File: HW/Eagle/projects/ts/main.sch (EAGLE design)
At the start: 29 parts, among them IC1 4050D, U1 ATMEGA328P-PU, U2 LM2576T, U3 HT7533

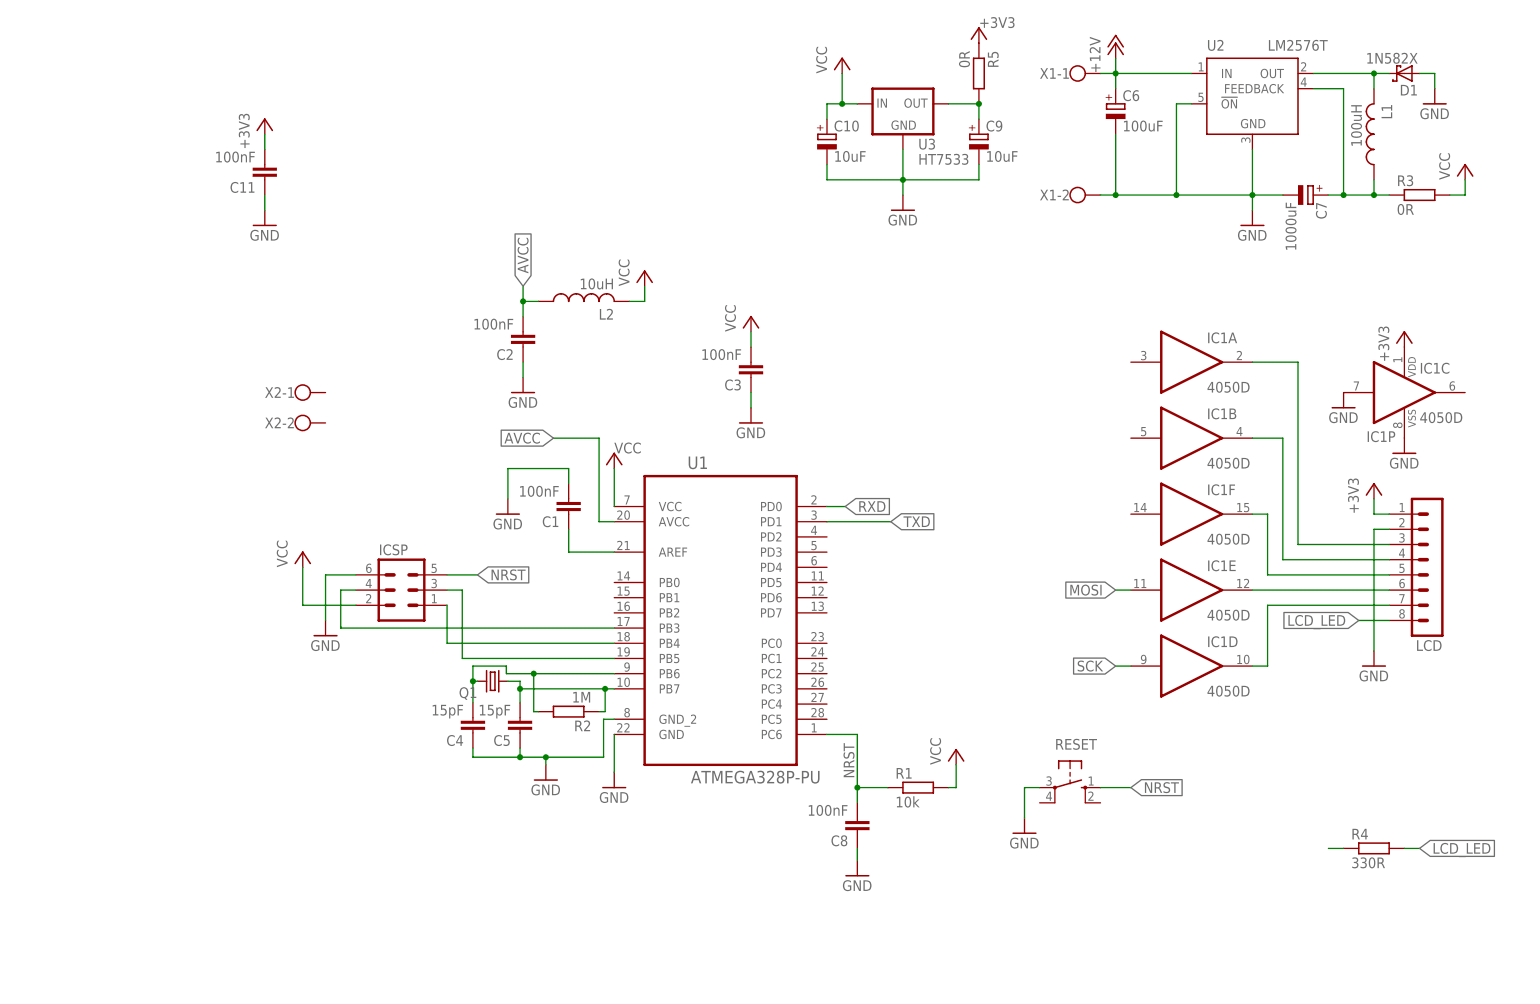
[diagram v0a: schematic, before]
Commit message: Commit before changing to digital temperature sensor
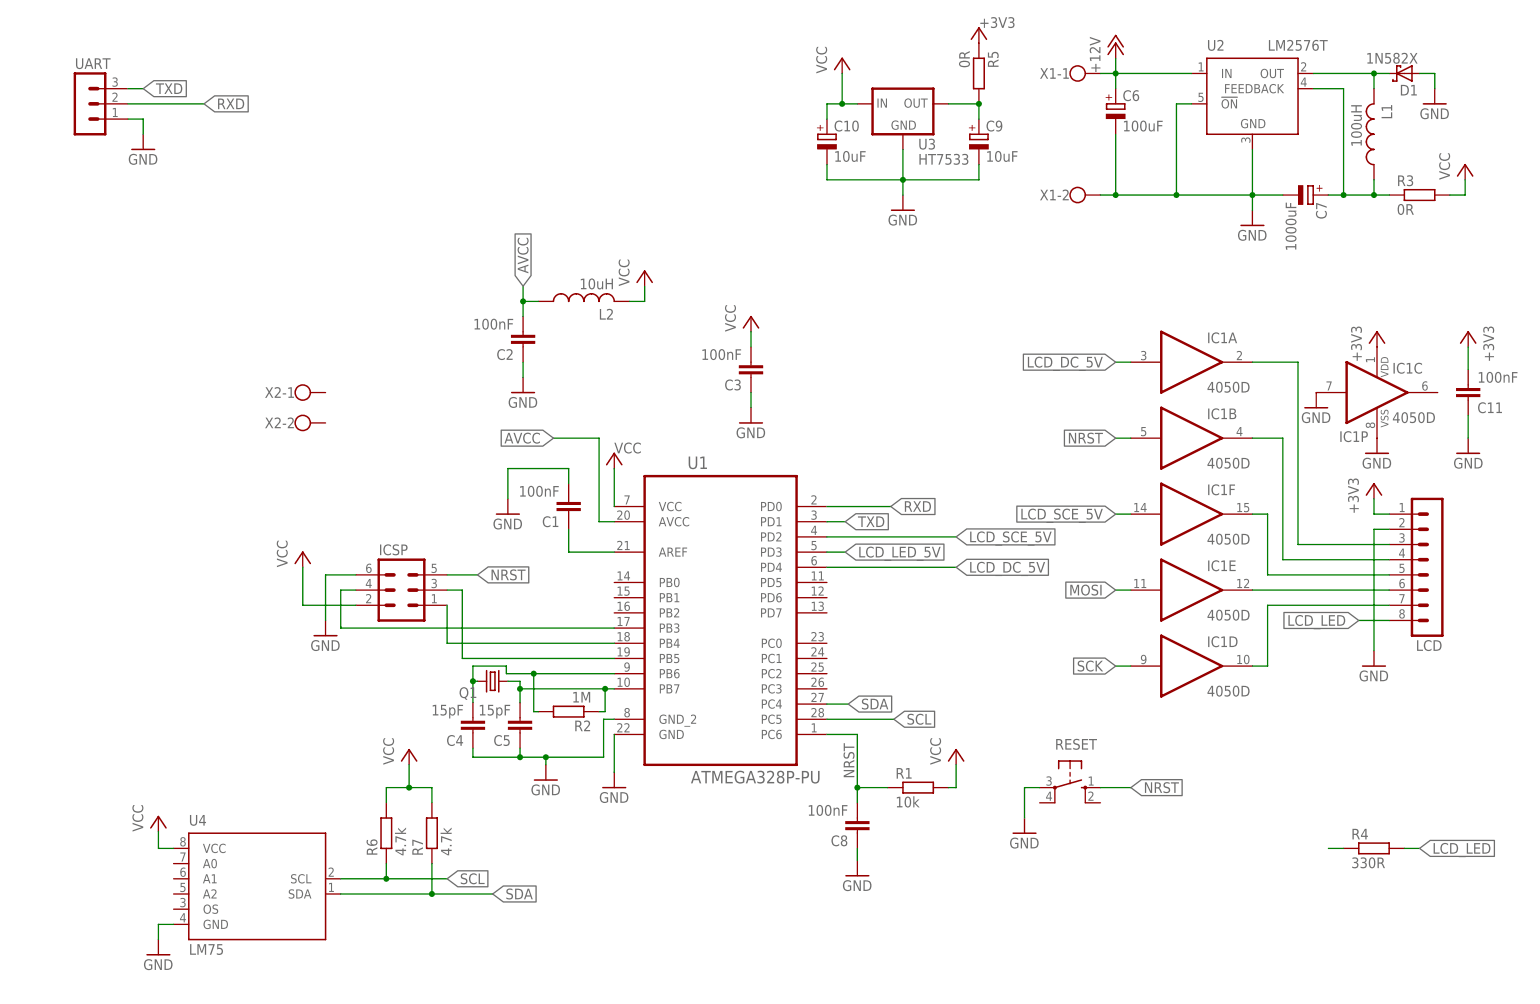
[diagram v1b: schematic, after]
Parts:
- added R6, R7: 4.7k, rcl:R-EU_R0805
- added U4: LM75, misc:LM75
- added UART: (no value), con-lstb:MA03-1
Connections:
- new net LCD_DC_5V: IC1A.I, U1.PD4
- new net LCD_LED_5V: U1.PD3
- new net LCD_SCE_5V: IC1F.I, U1.PD2
- new net SCL: R6.1, U1.PC5, U4.SCL
- new net SDA: R7.1, U1.PC4, U4.SDA
- net GND: now also U4.GND, UART.1
- net NRST: now also IC1B.I
- net RXD: now also UART.2
- net TXD: now also UART.3
- net VCC: now also R6.2, R7.2, U4.VCC
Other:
- moved on the sheet: C11, IC1C, IC1P
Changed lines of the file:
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@@
 <part name="GND14" library="supply1" deviceset="GND" device=""/>
 <part name="GND15" library="supply1" deviceset="GND" device=""/>
+<part name="UART" library="con-lstb" deviceset="MA03-1" device=""/>
+<part name="GND16" library="supply1" deviceset="GND" device=""/>
+<part name="U4" library="misc" deviceset="LM75" device=""/>
+<part name="R6" library="rcl" deviceset="R-EU_" device="R0805" value="4.7k"/>
+<part name="R7" library="rcl" deviceset="R-EU_" device="R0805" value="4.7k"/>
+<part name="P+9" library="supply1" deviceset="VCC" device=""/>
+<part name="P+10" library="supply1" deviceset="VCC" device=""/>
+<part name="GND17" library="supply1" deviceset="GND" device=""/>
 </parts>
 <sheets>
@@
 <instance part="IC1" gate="A" x="200.66" y="111.76"/>
 <instance part="IC1" gate="B" x="200.66" y="99.06"/>
-<instance part="IC1" gate="C" x="236.22" y="106.68"/>
+<instance part="IC1" gate="C" x="231.648" y="106.68"/>
 <instance part="IC1" gate="D" x="200.66" y="60.96"/>
 <instance part="IC1" gate="E" x="200.66" y="73.66"/>
 <instance part="IC1" gate="F" x="200.66" y="86.36"/>
-<instance part="IC1" gate="P" x="236.22" y="106.68" smashed="yes">
-<attribute name="NAME" x="229.87" y="98.425" size="1.778" layer="95"/>
+<instance part="IC1" gate="P" x="231.648" y="106.68" smashed="yes">
+<attribute name="NAME" x="225.298" y="98.425" size="1.778" layer="95"/>
 </instance>
-<instance part="GND9" gate="1" x="236.22" y="96.52"/>
-<instance part="+3V2" gate="G$1" x="236.22" y="116.84"/>
+<instance part="GND9" gate="1" x="231.648" y="96.52"/>
+<instance part="+3V2" gate="G$1" x="231.648" y="116.84"/>
 <instance part="LCD" gate="1" x="241.3" y="78.74" rot="R180"/>
 <instance part="+3V3" gate="G$1" x="231.14" y="91.44"/>
@@
 <instance part="GND11" gate="1" x="88.9" y="106.68"/>
 <instance part="GND12" gate="1" x="86.36" y="86.36"/>
-<instance part="C11" gate="G$1" x="45.72" y="142.24" rot="R180"/>
-<instance part="+3V4" gate="G$1" x="45.72" y="152.4"/>
-<instance part="GND13" gate="1" x="45.72" y="134.62"/>
+<instance part="C11" gate="G$1" x="246.888" y="105.41" rot="MR180"/>
+<instance part="+3V4" gate="G$1" x="246.888" y="116.84" rot="MR0"/>
+<instance part="GND13" gate="1" x="246.888" y="96.52" rot="MR0"/>
 <instance part="R4" gate="G$1" x="231.14" y="30.48"/>
 <instance part="RESET" gate="1" x="180.34" y="40.64" rot="R270"/>
 <instance part="GND14" gate="1" x="172.72" y="33.02"/>
-<instance part="GND15" gate="1" x="226.06" y="104.14"/>
+<instance part="GND15" gate="1" x="221.488" y="104.14"/>
+<instance part="UART" gate="G$1" x="15.24" y="154.94"/>
+<instance part="GND16" gate="1" x="25.4" y="147.32"/>
+<instance part="U4" gate="G$1" x="43.18" y="25.4"/>
+<instance part="R6" gate="G$1" x="66.04" y="33.02" rot="R90"/>
+<instance part="R7" gate="G$1" x="73.66" y="33.02" rot="R90"/>
+<instance part="P+9" gate="VCC" x="69.85" y="46.99"/>
+<instance part="P+10" gate="VCC" x="27.94" y="35.814"/>
+<instance part="GND17" gate="1" x="27.94" y="12.7"/>
 </instances>
 <busses>
@@
 <pinref part="C11" gate="G$1" pin="1"/>
 <pinref part="GND13" gate="1" pin="GND"/>
-<wire x1="45.72" y1="137.16" x2="45.72" y2="139.7" width="0.1524" layer="91"/>
+<wire x1="246.888" y1="99.06" x2="246.888" y2="102.87" width="0.1524" layer="91"/>
 </segment>
 <segment>
@@
 <pinref part="IC1" gate="C" pin="I"/>
 <pinref part="GND15" gate="1" pin="GND"/>
+</segment>
+<segment>
+<pinref part="UART" gate="G$1" pin="1"/>
+<pinref part="GND16" gate="1" pin="GND"/>
+<wire x1="22.86" y1="152.4" x2="25.4" y2="152.4" width="0.1524" layer="91"/>
+<wire x1="25.4" y1="152.4" x2="25.4" y2="149.86" width="0.1524" layer="91"/>
+</segment>
+<segment>
+<pinref part="GND17" gate="1" pin="GND"/>
+<pinref part="U4" gate="G$1" pin="GND"/>
+<wire x1="27.94" y1="15.24" x2="27.94" y2="17.78" width="0.1524" layer="91"/>
+<wire x1="27.94" y1="17.78" x2="30.48" y2="17.78" width="0.1524" layer="91"/>
 </segment>
 </net>
@@
 <wire x1="106.68" y1="121.92" x2="109.22" y2="121.92" width="0.1524" layer="91"/>
 <wire x1="109.22" y1="121.92" x2="109.22" y2="124.46" width="0.1524" layer="91"/>
+</segment>
+<segment>
+<pinref part="P+9" gate="VCC" pin="VCC"/>
+<wire x1="69.85" y1="44.45" x2="69.85" y2="40.64" width="0.1524" layer="91"/>
+<pinref part="R7" gate="G$1" pin="2"/>
+<wire x1="69.85" y1="40.64" x2="73.66" y2="40.64" width="0.1524" layer="91"/>
+<wire x1="73.66" y1="40.64" x2="73.66" y2="38.1" width="0.1524" layer="91"/>
+<pinref part="R6" gate="G$1" pin="2"/>
+<wire x1="69.85" y1="40.64" x2="66.04" y2="40.64" width="0.1524" layer="91"/>
+<wire x1="66.04" y1="40.64" x2="66.04" y2="38.1" width="0.1524" layer="91"/>
+<junction x="69.85" y="40.64"/>
+</segment>
+<segment>
+<pinref part="P+10" gate="VCC" pin="VCC"/>
+<pinref part="U4" gate="G$1" pin="VCC"/>
+<wire x1="27.94" y1="33.274" x2="27.94" y2="30.48" width="0.1524" layer="91"/>
+<wire x1="27.94" y1="30.48" x2="30.48" y2="30.48" width="0.1524" layer="91"/>
 </segment>
 </net>
@@
 <label x="190.5" y="40.64" size="1.778" layer="95" xref="yes"/>
 </segment>
+<segment>
+<pinref part="IC1" gate="B" pin="I"/>
+<wire x1="190.5" y1="99.06" x2="187.96" y2="99.06" width="0.1524" layer="91"/>
+<label x="187.96" y="99.06" size="1.778" layer="95" rot="R180" xref="yes"/>
+</segment>
 </net>
 <net name="N$7" class="0">
@@
 <pinref part="C11" gate="G$1" pin="2"/>
 <pinref part="+3V4" gate="G$1" pin="+3V3"/>
-<wire x1="45.72" y1="149.86" x2="45.72" y2="147.32" width="0.1524" layer="91"/>
+<wire x1="246.888" y1="114.3" x2="246.888" y2="110.49" width="0.1524" layer="91"/>
 </segment>
 </net>
@@
 <segment>
 <pinref part="U1" gate="A" pin="PD0"/>
-<wire x1="139.7" y1="87.63" x2="142.748" y2="87.63" width="0.1524" layer="91"/>
-<label x="142.748" y="87.63" size="1.778" layer="95" xref="yes"/>
+<wire x1="139.7" y1="87.63" x2="150.368" y2="87.63" width="0.1524" layer="91"/>
+<label x="150.368" y="87.63" size="1.778" layer="95" xref="yes"/>
+</segment>
+<segment>
+<pinref part="UART" gate="G$1" pin="2"/>
+<wire x1="22.86" y1="154.94" x2="35.56" y2="154.94" width="0.1524" layer="91"/>
+<label x="35.56" y="154.94" size="1.778" layer="95" xref="yes"/>
 </segment>
 </net>
@@
 <segment>
 <pinref part="U1" gate="A" pin="PD1"/>
-<wire x1="139.7" y1="85.09" x2="150.368" y2="85.09" width="0.1524" layer="91"/>
-<label x="150.368" y="85.09" size="1.778" layer="95" xref="yes"/>
+<wire x1="139.7" y1="85.09" x2="142.748" y2="85.09" width="0.1524" layer="91"/>
+<label x="142.748" y="85.09" size="1.778" layer="95" xref="yes"/>
+</segment>
+<segment>
+<pinref part="UART" gate="G$1" pin="3"/>
+<wire x1="22.86" y1="157.48" x2="25.4" y2="157.48" width="0.1524" layer="91"/>
+<label x="25.4" y="157.48" size="1.778" layer="95" xref="yes"/>
 </segment>
 </net>
@@
 </segment>
 </net>
+<net name="LCD_SCE_5V" class="0">
+<segment>
+<pinref part="U1" gate="A" pin="PD2"/>
+<wire x1="139.7" y1="82.55" x2="161.29" y2="82.55" width="0.1524" layer="91"/>
+<label x="161.29" y="82.55" size="1.778" layer="95" xref="yes"/>
+</segment>
+<segment>
+<pinref part="IC1" gate="F" pin="I"/>
+<wire x1="190.5" y1="86.36" x2="187.96" y2="86.36" width="0.1524" layer="91"/>
+<label x="187.96" y="86.36" size="1.778" layer="95" rot="R180" xref="yes"/>
+</segment>
+</net>
+<net name="LCD_DC_5V" class="0">
+<segment>
+<pinref part="U1" gate="A" pin="PD4"/>
+<wire x1="139.7" y1="77.47" x2="161.29" y2="77.47" width="0.1524" layer="91"/>
+<label x="161.29" y="77.47" size="1.778" layer="95" xref="yes"/>
+</segment>
+<segment>
+<pinref part="IC1" gate="A" pin="I"/>
+<wire x1="190.5" y1="111.76" x2="187.96" y2="111.76" width="0.1524" layer="91"/>
+<label x="187.96" y="111.76" size="1.778" layer="95" rot="R180" xref="yes"/>
+</segment>
+</net>
+<net name="LCD_LED_5V" class="0">
+<segment>
+<pinref part="U1" gate="A" pin="PD3"/>
+<wire x1="139.7" y1="80.01" x2="142.748" y2="80.01" width="0.1524" layer="91"/>
+<label x="142.748" y="80.01" size="1.778" layer="95" xref="yes"/>
+</segment>
+</net>
+<net name="SDA" class="0">
+<segment>
+<pinref part="U1" gate="A" pin="PC4"/>
+<wire x1="139.7" y1="54.61" x2="143.256" y2="54.61" width="0.1524" layer="91"/>
+<label x="143.256" y="54.61" size="1.778" layer="95" xref="yes"/>
+</segment>
+<segment>
+<pinref part="U4" gate="G$1" pin="SDA"/>
+<wire x1="58.42" y1="22.86" x2="73.66" y2="22.86" width="0.1524" layer="91"/>
+<pinref part="R7" gate="G$1" pin="1"/>
+<wire x1="73.66" y1="22.86" x2="83.82" y2="22.86" width="0.1524" layer="91"/>
+<wire x1="73.66" y1="27.94" x2="73.66" y2="22.86" width="0.1524" layer="91"/>
+<junction x="73.66" y="22.86"/>
+<label x="83.82" y="22.86" size="1.778" layer="95" xref="yes"/>
+</segment>
+</net>
+<net name="SCL" class="0">
+<segment>
+<pinref part="U1" gate="A" pin="PC5"/>
+<wire x1="139.7" y1="52.07" x2="150.876" y2="52.07" width="0.1524" layer="91"/>
+<label x="150.876" y="52.07" size="1.778" layer="95" xref="yes"/>
+</segment>
+<segment>
+<pinref part="U4" gate="G$1" pin="SCL"/>
+<wire x1="58.42" y1="25.4" x2="66.04" y2="25.4" width="0.1524" layer="91"/>
+<pinref part="R6" gate="G$1" pin="1"/>
+<wire x1="66.04" y1="25.4" x2="76.2" y2="25.4" width="0.1524" layer="91"/>
+<wire x1="66.04" y1="27.94" x2="66.04" y2="25.4" width="0.1524" layer="91"/>
+<junction x="66.04" y="25.4"/>
+<label x="76.2" y="25.4" size="1.778" layer="95" xref="yes"/>
+</segment>
+</net>

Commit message: Big Update
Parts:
- removed L2: 10uH, misc:FERRCORE
- added C12: 100nF, rcl:C-EUC0805
- added D2, D3: (no value), diode:DIODE-MINIMELF
- added KEYPAD: (no value), con-lstb:MA07-1
- added LED: (no value), jumper:JP1E
- added R10, R11: 10k, rcl:R-EU_R0805
- added R8: 4.7k, rcl:R-EU_R0805
- added R9: 330R, rcl:R-EU_R0805
- added T1, T2: IRLML2502, misc:IRLML2502
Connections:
- removed net AVCC: C2.2, L2.1, U1.AVCC
- new net KEYPAD_C0: KEYPAD.1, U1.PD7
- new net KEYPAD_C1: KEYPAD.2, U1.PD6
- new net KEYPAD_C2: KEYPAD.3, U1.PD5
- new net KEYPAD_R0: KEYPAD.4, U1.PC0
- new net KEYPAD_R1: KEYPAD.5, U1.PC1
- new net KEYPAD_R2: KEYPAD.6, U1.PC2
- new net KEYPAD_R3: KEYPAD.7, U1.PC3
- new net LED: LED.2, U1.PB2
- new net N$10: D2.A, T1.D, X2-1.KL
- new net N$11: D3.A, T2.D, X2-2.KL
- new net N$5: R8.1, U4.A0, U4.A1, U4.A2
- new net N$6: LED.1, R9.2
- new net OUT1: R10.2, T1.G, U1.PB0
- new net OUT2: R11.2, T2.G, U1.PB1
- net +12V: now also D2.C, D3.C
- net GND: now also C12.1, R10.1, R11.1, T1.S, T2.S
- net VCC: now also C12.2, C2.2, R8.2, R9.1, U1.AVCC; no longer L2.2
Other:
- moved on the sheet: C1, C11, C2, C3, C4, C5, C8, IC1A, IC1B, IC1C, IC1D, IC1E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
